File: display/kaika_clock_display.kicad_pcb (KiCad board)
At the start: 2 copper layers, 128 x 32 mm, 21 parts, among them J1 Conn_01x05, U1 MAX7219, U2 MAX7219, U3 MAX7219, U4 MAX7219, U5 LED-MATRIX-1088AS, U6 LED-MATRIX-1088AS, U7 LED-MATRIX-1088AS, U8 LED-MATRIX-1088AS

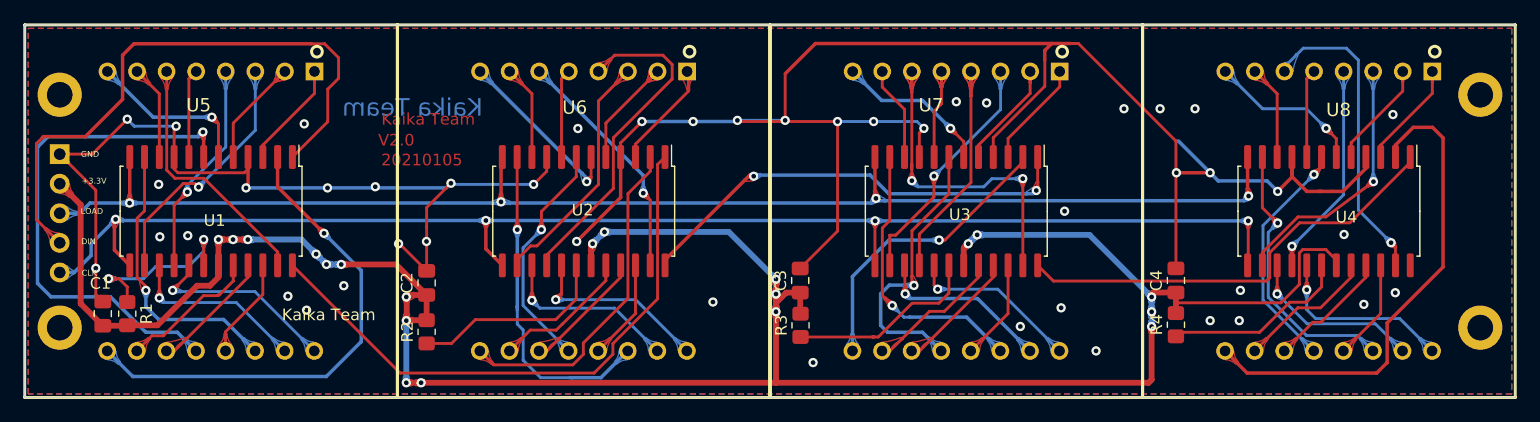
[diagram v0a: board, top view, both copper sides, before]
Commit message: modify the display
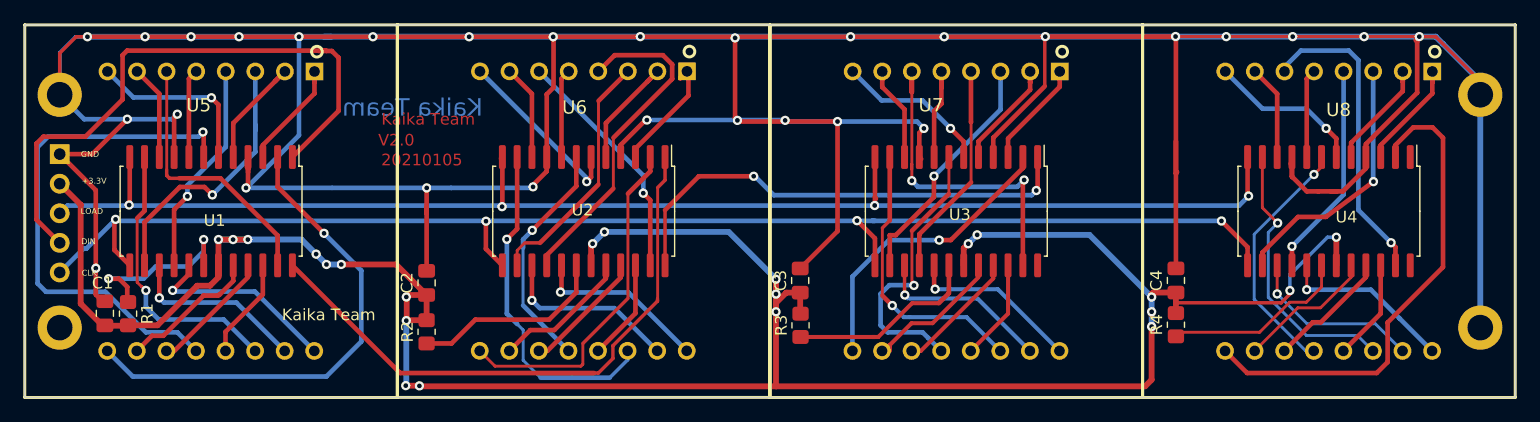
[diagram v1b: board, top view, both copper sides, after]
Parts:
- moved C1 0.18 mm to (106.9, 124.8)
- moved R1 0.07 mm to (108.9, 124.8)
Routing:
- net GND: track 237.9 -> 513.7 mm, vias 47 -> 29
- net Net-(U3-Pad24): track 38.5 -> 0.00 mm
- net Net-(U2-Pad24): track 39.2 -> 42.1 mm
- net VCC: track 215.6 -> 218.2 mm, vias 20 -> 22
- net 3_SEG_B: track 20.6 -> 18.6 mm
- net 1_SEG_A: track 21.8 -> 23.6 mm
- net CLK: track 122.2 -> 120.9 mm
- net 1_SEG_D: track 22.1 -> 23.2 mm
- net 2_SEG_G: track 16.2 -> 15.2 mm
- net 4_DIG_3: track 20.5 -> 21.6 mm
- net 2_DIG_1: track 28.7 -> 29.6 mm
- net LOAD: track 118.5 -> 119.3 mm
- net 2_DIG_4: track 10.9 -> 10.1 mm
- net 1_DIG_2: track 14.4 -> 15.2 mm
- net 2_DIG_0: track 29.1 -> 29.6 mm
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- removed copper zone on B.Cu, net GND
- removed copper zone on F.Cu, net GND

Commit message: modify the display
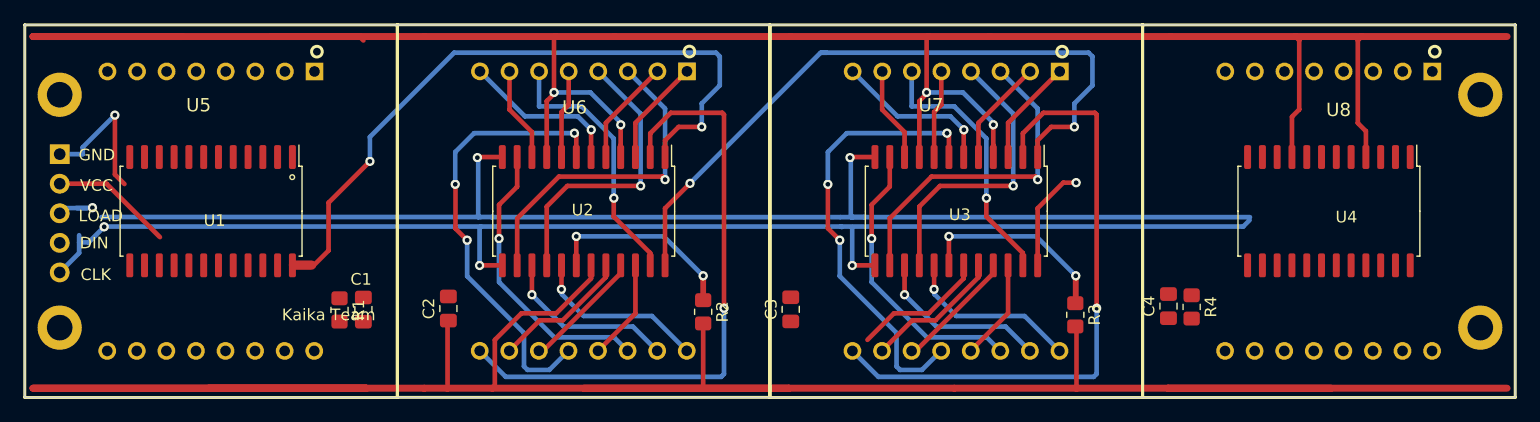
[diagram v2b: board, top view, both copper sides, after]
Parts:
- moved R2 23.8 mm to (158.3, 124.6), turned to 270 degrees
- moved R3 23.6 mm to (190.2, 124.9), turned to 270 degrees
- moved C1 22.2 mm to (129.1, 124.5)
- moved R1 18.2 mm to (127.0, 124.5)
- moved C2 2.89 mm to (136.4, 124.4)
- moved C3 2.60 mm to (165.8, 124.4)
- moved C4 2.29 mm to (198.2, 124.2)
- moved R4 2.04 mm to (200.2, 124.2), turned to 270 degrees
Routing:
- net GND: track 513.7 -> 225.2 mm, vias 29 -> 5
- net DIN: track 51.9 -> 0.00 mm
- net 1_DIG_3: track 44.6 -> 0.00 mm, vias 1 -> 0
- net 1_DIG_0: track 42.8 -> 0.00 mm, vias 1 -> 0
- net 4_DIG_0: track 42.5 -> 0.00 mm
- net VCC: track 218.2 -> 255.4 mm, vias 22 -> 0
- net 3_DIG_0: track 25.9 -> 53.6 mm
- net 4_SEG_D: track 26.6 -> 0.00 mm, vias 1 -> 0
- net 1_DIG_1: track 24.4 -> 0.00 mm, vias 1 -> 0
- net 2_DIG_0: track 29.6 -> 53.6 mm, vias 0 -> 1
- net 4_DIG_1: track 23.8 -> 0.00 mm, vias 1 -> 0
- net 1_SEG_A: track 23.6 -> 0.00 mm, vias 1 -> 0
- net 1_SEG_D: track 23.2 -> 0.00 mm
- net 4_SEG_A: track 22.4 -> 0.00 mm, vias 1 -> 0
- net 4_DIG_3: track 21.6 -> 0.00 mm, vias 1 -> 0
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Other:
- board text removed: "+3.3V"
- board text removed: "20210105"
- board text removed: "V2.0"

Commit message: 手工布线版本的显示板
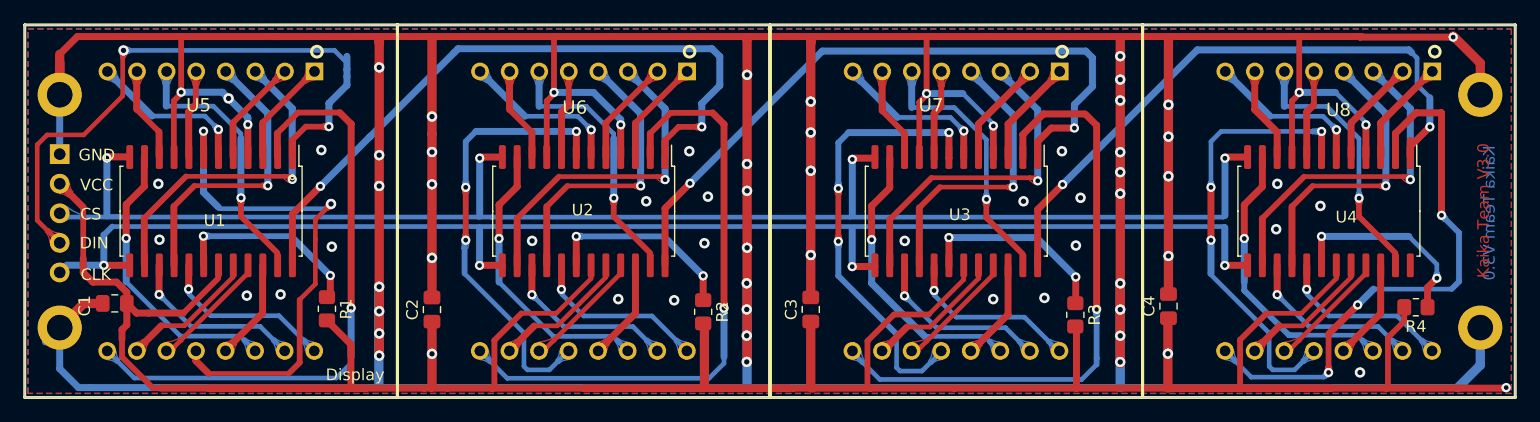
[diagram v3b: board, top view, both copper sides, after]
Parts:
- moved C1 21.4 mm to (107.7, 123.9), turned to 180 degrees
- moved R4 19.3 mm to (219.5, 124.2), turned to 180 degrees
- moved C3 1.72 mm to (167.5, 124.4)
- moved C2 1.41 mm to (135.0, 124.5)
- moved R1 1.08 mm to (126.0, 124.4)
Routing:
- net GND: track 225.2 -> 544.2 mm, vias 5 -> 71
- net DIN: track 0.00 -> 54.9 mm, vias 0 -> 2
- net 1_DIG_0: track 0.00 -> 52.7 mm, vias 0 -> 1
- net 4_DIG_0: track 0.00 -> 48.3 mm, vias 0 -> 3
- net Net-(U3-Pad24): track 9.11 -> 54.6 mm, vias 1 -> 2
- net 1_DIG_3: track 0.00 -> 44.7 mm, vias 0 -> 2
- net 4_DIG_3: track 0.00 -> 38.1 mm, vias 0 -> 3
- net VCC: track 255.4 -> 285.5 mm, vias 0 -> 3
- net 4_SEG_A: track 0.00 -> 29.0 mm, vias 0 -> 1
- net 1_SEG_A: track 0.00 -> 29.0 mm, vias 0 -> 1
- net 4_DIG_1: track 0.00 -> 25.3 mm, vias 0 -> 1
- net 1_SEG_B: track 0.00 -> 25.2 mm, vias 0 -> 1
- net 4_SEG_B: track 0.00 -> 25.2 mm, vias 0 -> 1
- net 1_DIG_1: track 0.00 -> 24.9 mm, vias 0 -> 1
- net 1_SEG_D: track 0.00 -> 23.0 mm, vias 0 -> 1
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- added copper zone on B.Cu, net GND
- added copper zone on F.Cu, net GND
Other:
- board text added: "CS"
- board text added: "Display"
- board text added: "Kaika Team V3.0"
- board text removed: "Kaika Team"
- board text removed: "Kaika Team V2.0"
- board text removed: "LOAD"

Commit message: modify the display
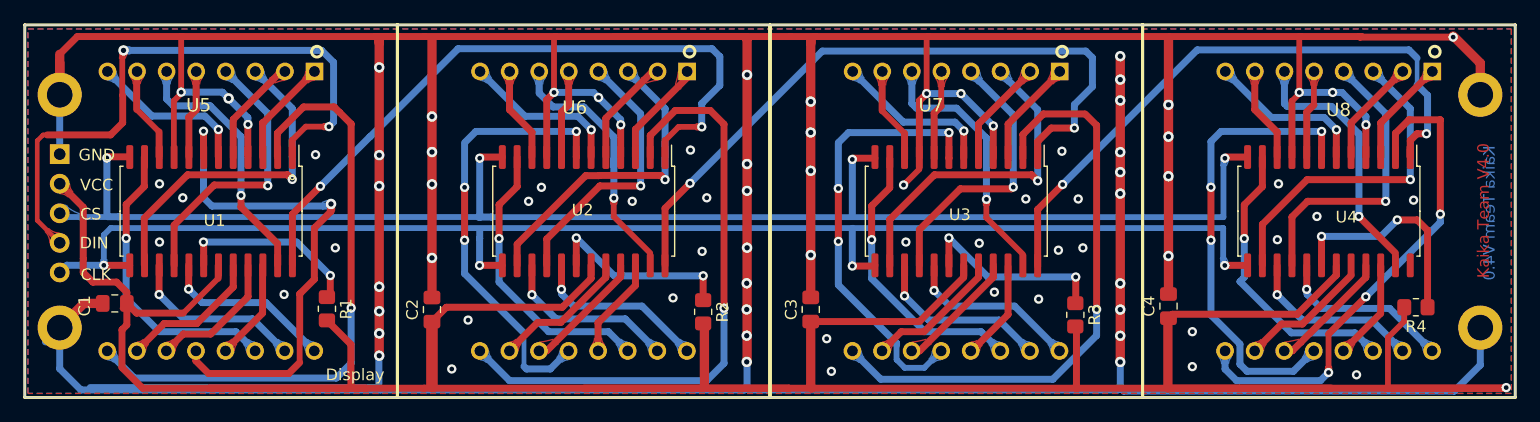
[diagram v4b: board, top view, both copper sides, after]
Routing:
- net GND: track 544.2 -> 584.5 mm, vias 71 -> 84
- net VCC: track 285.5 -> 298.8 mm, vias 3 -> 1
- net 4_DIG_0: track 48.3 -> 43.3 mm
- net DIN: track 54.9 -> 53.0 mm
- net 1_SEG_E: track 10.5 -> 12.3 mm
- net Net-(R4-Pad1): track 17.4 -> 19.1 mm
- net 2_SEG_B: track 25.2 -> 23.6 mm
- net 3_DIG_0: track 52.7 -> 51.2 mm
- net 4_DIG_3: track 38.1 -> 39.5 mm
- net 3_SEG_B: track 25.2 -> 24.0 mm
- net 2_SEG_A: track 29.0 -> 27.8 mm
- net 3_DIG_3: track 38.3 -> 37.4 mm
- net 1_SEG_B: track 25.2 -> 24.3 mm
- net 1_DIG_1: track 24.9 -> 25.7 mm
- net CLK: track 121.7 -> 120.9 mm
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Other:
- board text added: "Kaika Team V4.0"
- board text removed: "Kaika Team V3.0"

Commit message: modify the main
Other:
- board text added: "Kaika Team V4.2"
